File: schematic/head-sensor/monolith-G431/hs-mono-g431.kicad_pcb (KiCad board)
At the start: 2 copper layers, 78 x 41 mm, 55 parts, among them P1 MICROSD-SDIO-CD, P2 SWD, P3 G B Vcc, P4 NRF24L01, P5 USB_A, P6 SENSOR_CONNECTOR, P7 DEBUG_TX, Q1 IRLML6402, Q2 IRLML2502, Q3 IRLML2502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

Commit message: [PCB] Errors check in progress
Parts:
- D1: value Led -> Chrg
- D2: value LED -> DBG
- U5: value ITEAD_HC-05 -> HC-05

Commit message: [PCB] Final silk fixes for mono hs
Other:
- board text added: "RST IO CLK"
- board text added: "TX"
- board text added: "Vcc 3.3 S R G B Vib"
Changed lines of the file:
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@@
     (area -9.075001 -0.075001 69.075001 41.075001)
     (thickness 1.6)
-    (drawings 14)
+    (drawings 23)
     (tracks 724)
     (zones 0)
@@
     (descr "Through hole pin header")
     (tags "pin header")
-    (fp_text reference P3 (at 0 -5.1 90) (layer F.SilkS)
+    (fp_text reference P3 (at 0 -2.667 90) (layer F.SilkS)
       (effects (font (size 1 1) (thickness 0.15)))
     )
@@
     )
   )
+  (gr_text "Vcc 3.3 S  R  G  B Vib" (at 31.4325 5.3975) (layer F.SilkS)
+    (effects (font (size 1 1) (thickness 0.15)) (justify left))
+  )
+  (gr_line (start 30.226 5.2705) (end 30.226 5.9055) (angle 90) (layer F.SilkS) (width 0.2))
+  (gr_line (start 29.9085 5.9055) (end 30.5435 5.9055) (angle 90) (layer F.SilkS) (width 0.2))
+  (gr_text TX (at 1.27 32.1945) (layer F.SilkS)
+    (effects (font (size 1 1) (thickness 0.15)))
+  )
+  (gr_text "RST IO CLK" (at 3.7465 27.686) (layer F.SilkS)
+    (effects (font (size 1 1) (thickness 0.15)))
+  )
+  (gr_line (start -2.0955 31.9405) (end -2.0955 32.5755) (angle 90) (layer F.SilkS) (width 0.2))
+  (gr_line (start -2.413 32.5755) (end -1.778 32.5755) (angle 90) (layer F.SilkS) (width 0.2))
+  (gr_line (start -2.413 28.0035) (end -1.778 28.0035) (angle 90) (layer F.SilkS) (width 0.2))
+  (gr_line (start -2.0955 27.3685) (end -2.0955 28.0035) (angle 90) (layer F.SilkS) (width 0.2))
   (gr_line (start 52.1335 34) (end 60 34) (angle 90) (layer Edge.Cuts) (width 0.15))
   (gr_line (start 52.1335 23.5) (end 52.1335 34) (angle 90) (layer Edge.Cuts) (width 0.15))

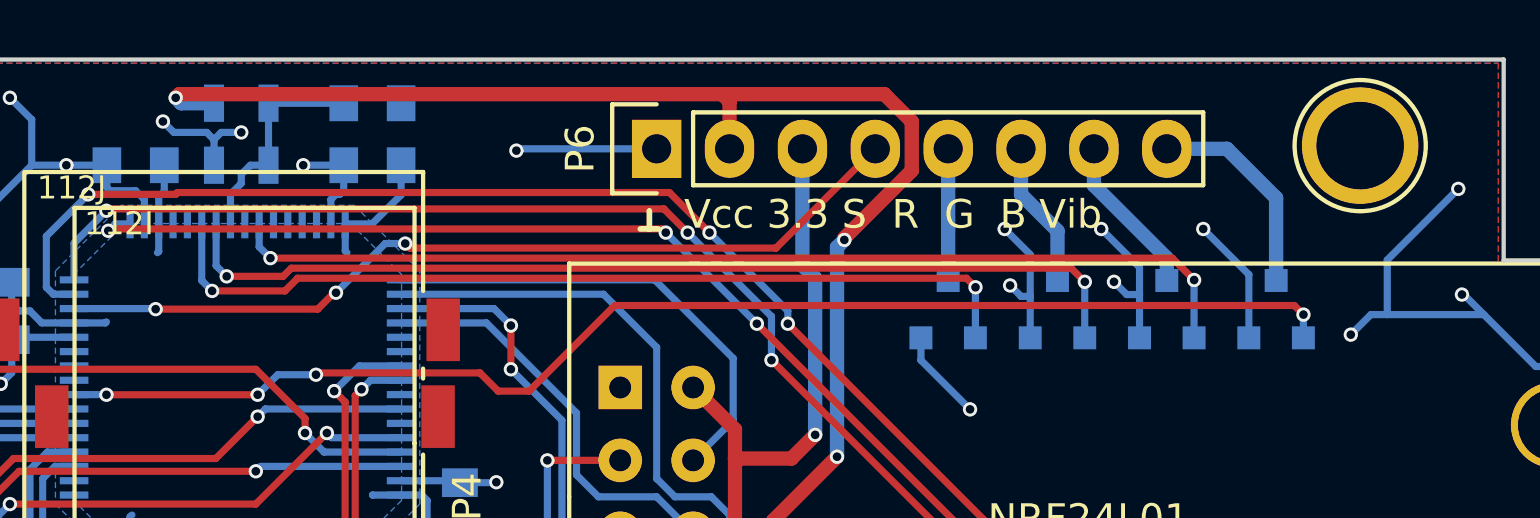
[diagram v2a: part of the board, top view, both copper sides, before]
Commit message: [PCB] Head sensor fix: added UART/I2C pins to sensors connector
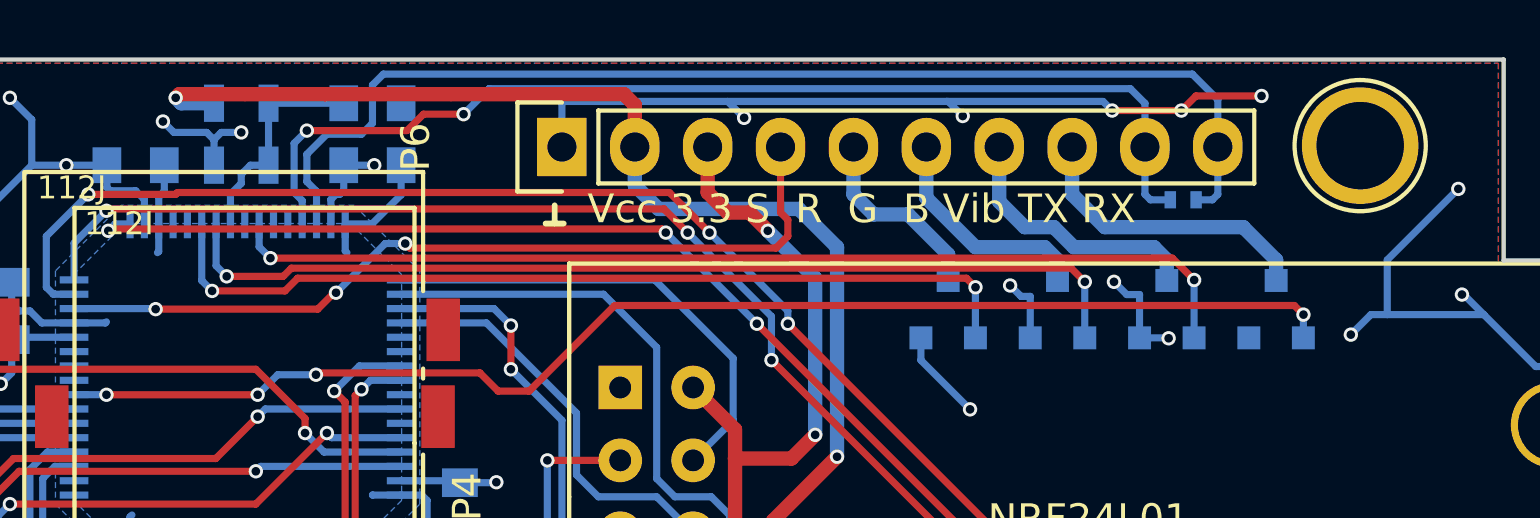
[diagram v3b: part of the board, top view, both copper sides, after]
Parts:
- added JP1: Jumper_NO_Small, Resistors_SMD:R_0402, B.Cu at (48.8, 4.89)
- added REF***: OSHW-Logo2_14.6x12mm_SilkScreen, Symbols:OSHW-Logo2_14.6x12mm_SilkScreen, B.Cu at (37.1, 28.5)
- P6: footprint Pin_Headers:Pin_Header_Straight_1x08 -> Pin_Headers:Pin_Header_Straight_1x10
- moved P6 3.30 mm to (27.2, 3.05)
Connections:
- U1 pad 29: Net-(U1-Pad29) -> Net-(JP1-Pad1)
- U1 pad 30: Net-(U1-Pad30) -> Net-(JP1-Pad2)
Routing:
- net Net-(JP1-Pad2): track 0.00 -> 40.8 mm
- net Net-(JP1-Pad1): track 0.00 -> 37.7 mm, vias 0 -> 2
- net GND: track 203.6 -> 217.3 mm, vias 47 -> 49
- net VCC: track 115.2 -> 108.6 mm, vias 9 -> 8
- net Net-(P6-Pad7): track 5.64 -> 9.30 mm
- net Net-(P6-Pad8): track 7.40 -> 10.4 mm
- net Net-(P6-Pad6): track 5.12 -> 7.96 mm
- net Net-(P6-Pad5): track 4.59 -> 6.73 mm
- net +3V3: track 111.6 -> 113.4 mm, vias 4 -> 5
- net Net-(P6-Pad4): track 30.4 -> 29.3 mm
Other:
- board text added: "Caustic Head Sensor G431 box rev.2 ltcaustic.org"
- board text added: "Vcc 3.3 S R G B Vib TX RX"
- board text removed: "Vcc 3.3 S R G B Vib"
